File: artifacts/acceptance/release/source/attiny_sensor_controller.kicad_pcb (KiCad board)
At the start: 2 copper layers, 45 x 30 mm, 10 parts, among them J1 QWIIC, J2 UPDI_VTREF_SENSE, U1 ATtiny402-SS, U2 TMP102B

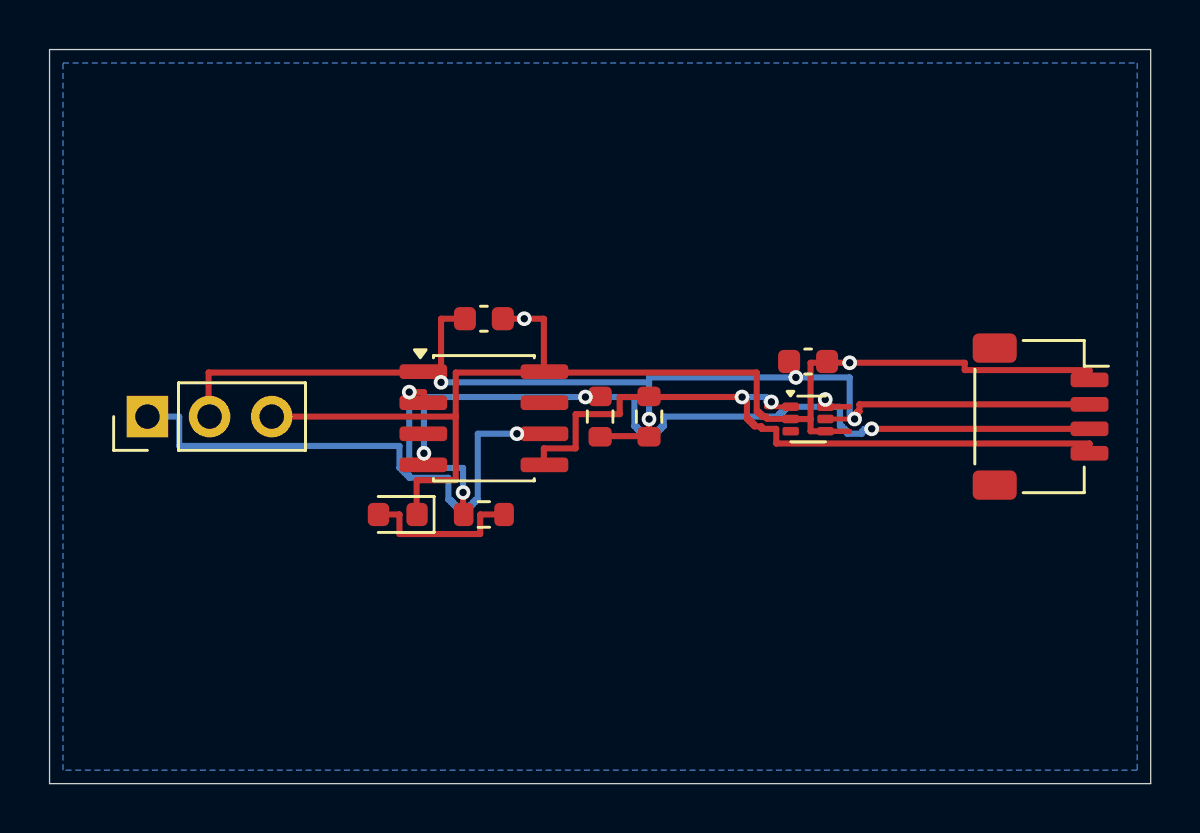
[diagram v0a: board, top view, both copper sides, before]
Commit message: refactor: rename PCB Agent to CopperWright
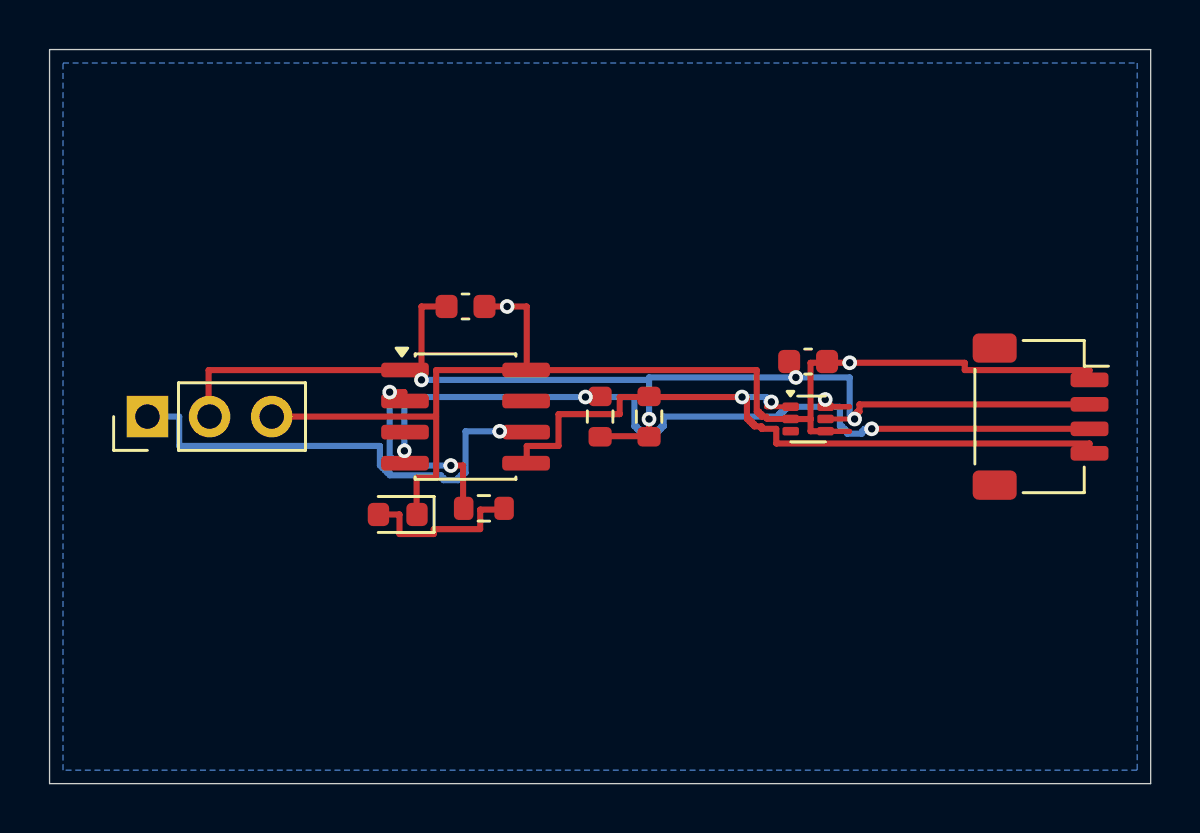
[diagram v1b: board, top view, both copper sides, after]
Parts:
- moved C1 0.90 mm to (17.0, 10.5)
- moved U1 0.75 mm to (17.0, 15.0)
- moved R3 0.25 mm to (17.8, 18.8)
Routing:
- net /UPDI: track 22.9 -> 20.1 mm
- net /I2C_SDA: track 37.1 -> 37.8 mm
- net /I2C_SCL: track 30.2 -> 30.8 mm
- net /LED_CTRL: track 8.20 -> 8.80 mm
